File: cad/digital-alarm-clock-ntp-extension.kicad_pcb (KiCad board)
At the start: 2 copper layers, 71.1 x 48.3 mm, 16 parts, among them J1 DigitalClock, J2 Power, J3 M5ATOM Left side, J4 M5ATOM Right side, Q1 2SC1815, Q2 2SC1815, Q3 2SC1815, Q4 2SC1815

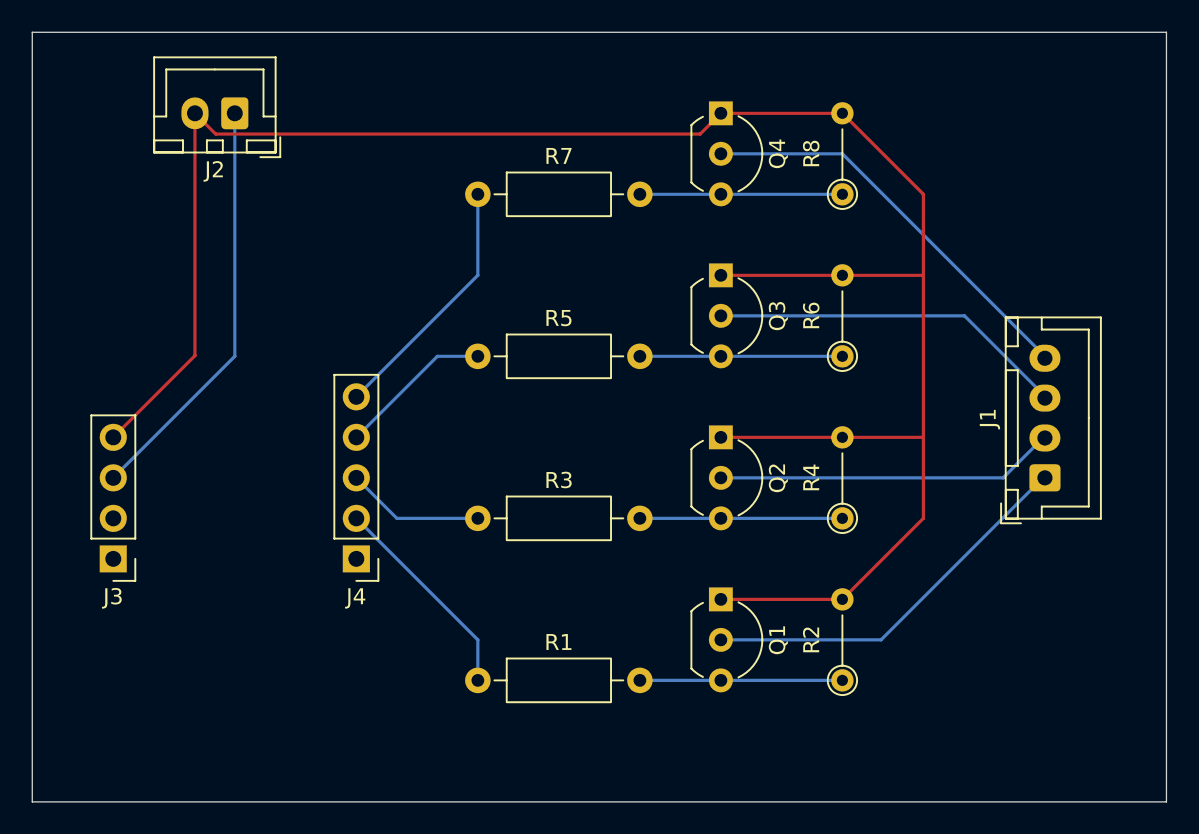
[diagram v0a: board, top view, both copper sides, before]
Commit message: feat: 回路図、基板のピンアサインの修正
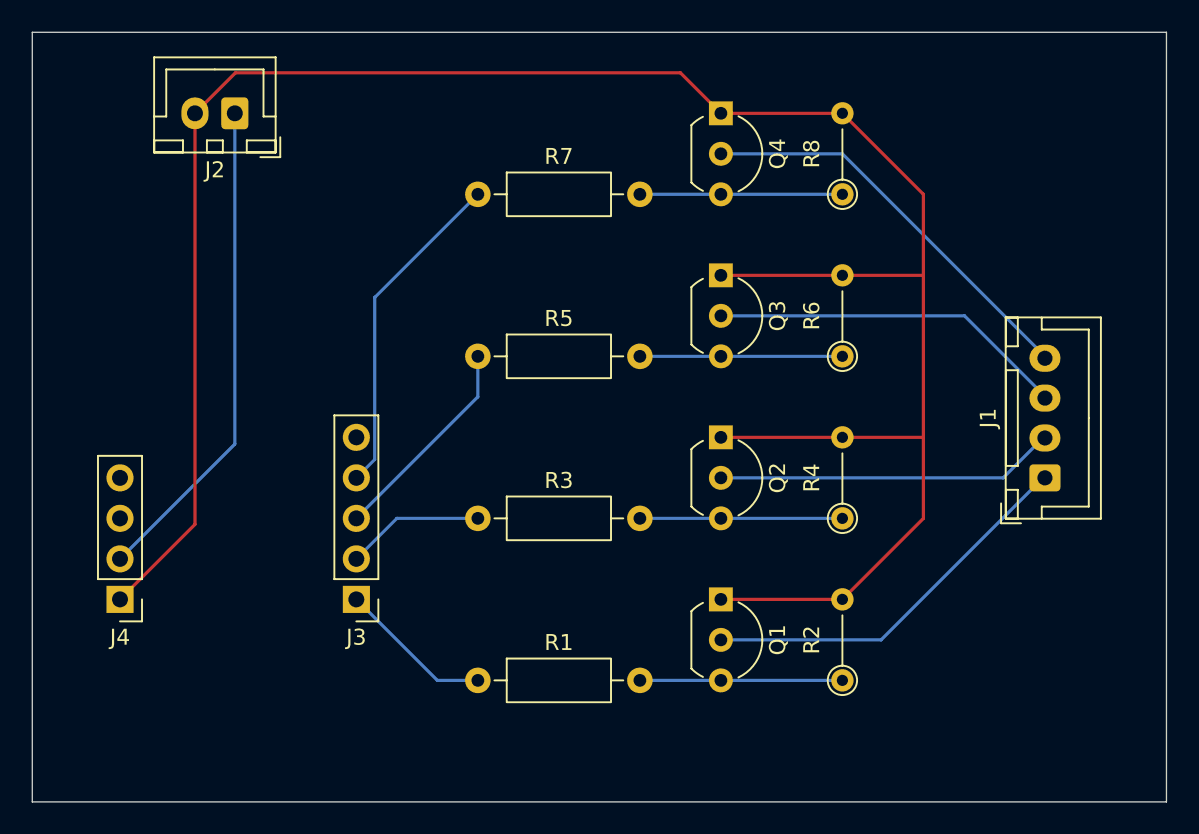
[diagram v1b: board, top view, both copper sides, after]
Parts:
- moved J4 2.57 mm to (119.8, 111.8)
- moved J3 2.54 mm to (134.6, 111.8)
- renumbered J4 to J3, J3 to J4
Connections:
- J3 pad 1: unconnected-(J4-Pin_1-Pad1) -> G33
- J3 pad 2: G22 -> G23
- J3 pad 4: G23 -> G22
- J3 pad 5: G33 -> unconnected-(J3-Pin_5-Pad5)
- J4 pad 1: unconnected-(J3-Pin_1-Pad1) -> GND
- J4 pad 2: unconnected-(J3-Pin_2-Pad2) -> +5V
- J4 pad 3: +5V -> unconnected-(J4-Pin_3-Pad3)
- J4 pad 4: GND -> unconnected-(J4-Pin_4-Pad4)
- R1 pad 1: G22 -> G33
- R3 pad 1: G19 -> G23
- R5 pad 1: G23 -> G19
- R7 pad 1: G33 -> G22
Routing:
- net GND: track 131.8 -> 142.8 mm
- net G22: track 13.3 -> 20.9 mm
- net G33: track 15.9 -> 9.72 mm
- net +5V: track 26.0 -> 30.9 mm
- net G19: track 8.67 -> 13.3 mm
- net G23: track 9.72 -> 8.67 mm
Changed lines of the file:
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@@
 	(net 4 "BTN_1_SET")
 	(net 5 "GND")
-	(net 6 "unconnected-(J3-Pin_1-Pad1)")
-	(net 7 "G33")
-	(net 8 "G19")
-	(net 9 "G23")
-	(net 10 "G22")
-	(net 11 "Net-(Q1-B)")
-	(net 12 "Net-(Q2-B)")
-	(net 13 "Net-(Q3-B)")
-	(net 14 "Net-(Q4-B)")
-	(net 15 "+5V")
-	(net 16 "unconnected-(J3-Pin_2-Pad2)")
-	(net 17 "unconnected-(J4-Pin_1-Pad1)")
+	(net 6 "G33")
+	(net 7 "G19")
+	(net 8 "G23")
+	(net 9 "G22")
+	(net 10 "Net-(Q1-B)")
+	(net 11 "Net-(Q2-B)")
+	(net 12 "Net-(Q3-B)")
+	(net 13 "Net-(Q4-B)")
+	(net 14 "+5V")
+	(net 15 "unconnected-(J4-Pin_4-Pad4)")
+	(net 16 "unconnected-(J4-Pin_3-Pad3)")
+	(net 17 "unconnected-(J3-Pin_5-Pad5)")
 	(footprint "Resistor_THT:R_Axial_DIN0204_L3.6mm_D1.6mm_P5.08mm_Vertical"
 		(layer "F.Cu")
@@
 			(layers "*.Cu" "*.Mask")
 			(remove_unused_layers no)
-			(net 13 "Net-(Q3-B)")
+			(net 12 "Net-(Q3-B)")
 			(pintype "passive")
 		)
@@
 	(footprint "Connector_PinHeader_2.54mm:PinHeader_1x04_P2.54mm_Vertical"
 		(layer "F.Cu")
-		(at 119.38 109.22 180)
+		(at 119.8 111.76 180)
 		(descr "Through hole straight pin header, 1x04, 2.54mm pitch, single row")
 		(tags "Through hole pin header THT 1x04 2.54mm single row")
-		(property "Reference" "J3"
+		(property "Reference" "J4"
 			(at 0 -2.38 0)
 			(layer "F.SilkS")
@@
 			(layers "*.Cu" "*.Mask")
 			(remove_unused_layers no)
-			(net 6 "unconnected-(J3-Pin_1-Pad1)")
+			(net 5 "GND")
 			(pinfunction "Pin_1")
-			(pintype "passive+no_connect")
+			(pintype "passive")
 		)
 		(pad "2" thru_hole circle
@@
 			(layers "*.Cu" "*.Mask")
 			(remove_unused_layers no)
-			(net 16 "unconnected-(J3-Pin_2-Pad2)")
+			(net 14 "+5V")
 			(pinfunction "Pin_2")
-			(pintype "passive+no_connect")
+			(pintype "passive")
 		)
 		(pad "3" thru_hole circle
@@
 			(layers "*.Cu" "*.Mask")
 			(remove_unused_layers no)
-			(net 15 "+5V")
+			(net 16 "unconnected-(J4-Pin_3-Pad3)")
 			(pinfunction "Pin_3")
-			(pintype "passive")
+			(pintype "passive+no_connect")
 		)
 		(pad "4" thru_hole circle
@@
 			(layers "*.Cu" "*.Mask")
 			(remove_unused_layers no)
-			(net 5 "GND")
+			(net 15 "unconnected-(J4-Pin_4-Pad4)")
 			(pinfunction "Pin_4")
-			(pintype "passive")
+			(pintype "passive+no_connect")
 		)
 		(embedded_fonts no)
@@
 			(layers "*.Cu" "*.Mask")
 			(remove_unused_layers no)
-			(net 14 "Net-(Q4-B)")
+			(net 13 "Net-(Q4-B)")
 			(pinfunction "B")
 			(pintype "input")
@@
 			(layers "*.Cu" "*.Mask")
 			(remove_unused_layers no)
-			(net 7 "G33")
+			(net 9 "G22")
 			(pintype "passive")
 		)
@@
 			(layers "*.Cu" "*.Mask")
 			(remove_unused_layers no)
-			(net 14 "Net-(Q4-B)")
+			(net 13 "Net-(Q4-B)")
 			(pintype "passive")
 		)
@@
 			(layers "*.Cu" "*.Mask")
 			(remove_unused_layers no)
-			(net 12 "Net-(Q2-B)")
+			(net 11 "Net-(Q2-B)")
 			(pintype "passive")
 		)
@@
 			(layers "*.Cu" "*.Mask")
 			(remove_unused_layers no)
-			(net 14 "Net-(Q4-B)")
+			(net 13 "Net-(Q4-B)")
 			(pintype "passive")
 		)
@@
 			(layers "*.Cu" "*.Mask")
 			(remove_unused_layers no)
-			(net 10 "G22")
+			(net 6 "G33")
 			(pintype "passive")
 		)
@@
 			(layers "*.Cu" "*.Mask")
 			(remove_unused_layers no)
-			(net 11 "Net-(Q1-B)")
+			(net 10 "Net-(Q1-B)")
 			(pintype "passive")
 		)
@@
 			(layers "*.Cu" "*.Mask")
 			(remove_unused_layers no)
-			(net 11 "Net-(Q1-B)")
+			(net 10 "Net-(Q1-B)")
 			(pintype "passive")
 		)
@@
 			(layers "*.Cu" "*.Mask")
 			(remove_unused_layers no)
-			(net 12 "Net-(Q2-B)")
+			(net 11 "Net-(Q2-B)")
 			(pinfunction "B")
 			(pintype "input")
@@
 			(layers "*.Cu" "*.Mask")
 			(remove_unused_layers no)
-			(net 8 "G19")
+			(net 8 "G23")
 			(pintype "passive")
 		)
@@
 			(layers "*.Cu" "*.Mask")
 			(remove_unused_layers no)
-			(net 12 "Net-(Q2-B)")
+			(net 11 "Net-(Q2-B)")
 			(pintype "passive")
 		)
@@
 			(layers "*.Cu" "*.Mask")
 			(remove_unused_layers no)
-			(net 11 "Net-(Q1-B)")
+			(net 10 "Net-(Q1-B)")
 			(pinfunction "B")
 			(pintype "input")
@@
 			(layers "*.Cu" "*.Mask")
 			(remove_unused_layers no)
-			(net 13 "Net-(Q3-B)")
+			(net 12 "Net-(Q3-B)")
 			(pinfunction "B")
 			(pintype "input")
@@
 			(layers "*.Cu" "*.Mask")
 			(remove_unused_layers no)
-			(net 9 "G23")
+			(net 7 "G19")
 			(pintype "passive")
 		)
@@
 			(layers "*.Cu" "*.Mask")
 			(remove_unused_layers no)
-			(net 13 "Net-(Q3-B)")
+			(net 12 "Net-(Q3-B)")
 			(pintype "passive")
 		)
@@
 			(remove_unused_layers no)
 			(roundrect_rratio 0.147059)
-			(net 15 "+5V")
+			(net 14 "+5V")
 			(pinfunction "Pin_1")
 			(pintype "passive")
@@
 	(footprint "Connector_PinHeader_2.54mm:PinHeader_1x05_P2.54mm_Vertical"
 		(layer "F.Cu")
-		(at 134.62 109.22 180)
+		(at 134.62 111.76 180)
 		(descr "Through hole straight pin header, 1x05, 2.54mm pitch, single row")
 		(tags "Through hole pin header THT 1x05 2.54mm single row")
-		(property "Reference" "J4"
+		(property "Reference" "J3"
 			(at 0 -2.38 0)
 			(layer "F.SilkS")
@@
 			(layers "*.Cu" "*.Mask")
 			(remove_unused_layers no)
-			(net 17 "unconnected-(J4-Pin_1-Pad1)")
+			(net 6 "G33")
 			(pinfunction "Pin_1")
-			(pintype "passive+no_connect")
+			(pintype "passive")
 		)
 		(pad "2" thru_hole circle
@@
 			(layers "*.Cu" "*.Mask")
 			(remove_unused_layers no)
-			(net 10 "G22")
+			(net 8 "G23")
 			(pinfunction "Pin_2")
 			(pintype "passive")
@@
 			(layers "*.Cu" "*.Mask")
 			(remove_unused_layers no)
-			(net 8 "G19")
+			(net 7 "G19")
 			(pinfunction "Pin_3")
 			(pintype "passive")
@@
 			(layers "*.Cu" "*.Mask")
 			(remove_unused_layers no)
-			(net 9 "G23")
+			(net 9 "G22")
 			(pinfunction "Pin_4")
 			(pintype "passive")
@@
 			(layers "*.Cu" "*.Mask")
 			(remove_unused_layers no)
-			(net 7 "G33")
+			(net 17 "unconnected-(J3-Pin_5-Pad5)")
 			(pinfunction "Pin_5")
-			(pintype "passive")
+			(pintype "passive+no_connect")
 		)
 		(embedded_fonts no)
@@
 	)
 	(segment
-		(start 170.18 86.36)
-		(end 170.18 91.44)
+		(start 124.5 107.06)
+		(end 119.8 111.76)
 		(width 0.2)
 		(layer "F.Cu")
@@
 	)
 	(segment
-		(start 156.179 82.581)
-		(end 125.801 82.581)
+		(start 170.18 86.36)
+		(end 170.18 91.44)
 		(width 0.2)
 		(layer "F.Cu")
@@
 	)
 	(segment
-		(start 124.5 81.28)
-		(end 124.5 96.48)
-		(width 0.2)
-		(layer "F.Cu")
-		(net 5)
-	)
-	(segment
-		(start 124.5 96.48)
-		(end 119.38 101.6)
+		(start 165.1 81.28)
+		(end 170.18 86.36)
 		(width 0.2)
 		(layer "F.Cu")
@@
 	)
 	(segment
-		(start 165.1 81.28)
-		(end 170.18 86.36)
+		(start 157.48 81.28)
+		(end 154.94 78.74)
 		(width 0.2)
 		(layer "F.Cu")
@@
 	)
 	(segment
-		(start 125.801 82.581)
-		(end 124.5 81.28)
+		(start 124.5 81.28)
+		(end 124.5 107.06)
 		(width 0.2)
 		(layer "F.Cu")
@@
 	)
 	(segment
-		(start 157.48 81.28)
-		(end 156.179 82.581)
+		(start 127.04 78.74)
+		(end 124.5 81.28)
+		(width 0.2)
+		(layer "F.Cu")
+		(net 5)
+	)
+	(segment
+		(start 154.94 78.74)
+		(end 127.04 78.74)
 		(width 0.2)
 		(layer "F.Cu")
@@
 	)
 	(segment
-		(start 142.24 91.44)
-		(end 134.62 99.06)
+		(start 142.24 116.84)
+		(end 139.7 116.84)
+		(width 0.2)
+		(layer "B.Cu")
+		(net 6)
+	)
+	(segment
+		(start 139.7 116.84)
+		(end 134.62 111.76)
+		(width 0.2)
+		(layer "B.Cu")
+		(net 6)
+	)
+	(segment
+		(start 142.24 99.06)
+		(end 134.62 106.68)
 		(width 0.2)
 		(layer "B.Cu")
@@
 	)
 	(segment
-		(start 142.24 86.36)
-		(end 142.24 91.44)
+		(start 142.24 96.52)
+		(end 142.24 99.06)
 		(width 0.2)
 		(layer "B.Cu")
@@
 	(segment
 		(start 137.16 106.68)
-		(end 134.62 104.14)
+		(end 134.62 109.22)
 		(width 0.2)
 		(layer "B.Cu")
@@
 	)
 	(segment
-		(start 142.24 96.52)
-		(end 139.7 96.52)
+		(start 135.771 102.989)
+		(end 134.62 104.14)
 		(width 0.2)
 		(layer "B.Cu")
@@
 	)
 	(segment
-		(start 139.7 96.52)
-		(end 134.62 101.6)
+		(start 135.771 92.829)
+		(end 135.771 102.989)
 		(width 0.2)
 		(layer "B.Cu")
@@
 	)
 	(segment
-		(start 142.24 114.3)
-		(end 142.24 116.84)
-		(width 0.2)
-		(layer "B.Cu")
-		(net 10)
-	)
-	(segment
-		(start 134.62 106.68)
-		(end 142.24 114.3)
+		(start 142.24 86.36)
+		(end 135.771 92.829)
 		(width 0.2)
 		(layer "B.Cu")
-		(net 10)
+		(net 9)
 	)
 	(segment
@@
 		(width 0.2)
 		(layer "B.Cu")
-		(net 11)
+		(net 10)
 	)
 	(segment
@@
 		(width 0.2)
 		(layer "B.Cu")
-		(net 12)
+		(net 11)
 	)
 	(segment
@@
 		(width 0.2)
 		(layer "B.Cu")
-		(net 13)
+		(net 12)
 	)
 	(segment
@@
 		(width 0.2)
 		(layer "B.Cu")
-		(net 14)
+		(net 13)
 	)
 	(segment
-		(start 127 96.52)
-		(end 119.38 104.14)
+		(start 127 81.28)
+		(end 127 102.02)
 		(width 0.2)
 		(layer "B.Cu")
-		(net 15)
+		(net 14)
 	)
 	(segment
-		(start 127 81.28)
-		(end 127 96.52)
+		(start 127 102.02)
+		(end 119.8 109.22)
 		(width 0.2)
 		(layer "B.Cu")
-		(net 15)
+		(net 14)
 	)
 	(embedded_fonts no)
